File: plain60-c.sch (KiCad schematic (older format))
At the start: 176 parts, among them J1 HRO-TYPE-C-31-M-12, J2 ISP, K1 KEYSW, K10 KEYSW, K11 KEYSW, K12 KEYSW, K13 KEYSW, K14 KEYSW, K15 KEYSW, K15-1 KEYSW, K16 KEYSW, K17 KEYSW, K18 KEYSW, K19 KEYSW, K2 KEYSW, K20 KEYSW, K21 KEYSW, K22 KEYSW, K23 KEYSW, K24 KEYSW, K25 KEYSW, K26 KEYSW, K27 KEYSW, K28 KEYSW, K29 KEYSW, K3 KEYSW, K31 KEYSW, K31-1 KEYSW, K32 KEYSW, K33 KEYSW, K34 KEYSW, K35 KEYSW, K36 KEYSW, K37 KEYSW, K38 KEYSW, K39 KEYSW, K4 KEYSW, K40 KEYSW, K41 KEYSW, K42 KEYSW, K43 KEYSW, K44 KEYSW, K44-1 KEYSW, K46 KEYSW, K46-1 KEYSW, K47 KEYSW, K48 KEYSW, K49 KEYSW, K5 KEYSW, K50 KEYSW, K51 KEYSW, K52 KEYSW, K53 KEYSW, K54 KEYSW, K55 KEYSW, K56 KEYSW, K57 KEYSW, K58 KEYSW, K58-1 KEYSW, K59 KEYSW, K6 KEYSW, K61 KEYSW, K61-1 KEYSW, K62 KEYSW, K62-1 KEYSW, K63 KEYSW, K63-1 KEYSW, K67 KEYSW, K67-1 KEYSW, K7 KEYSW, K71 KEYSW, K72 KEYSW, K72-1 KEYSW, K73 KEYSW, K73-1 KEYSW, K74 KEYSW, K74-1 KEYSW, K8 KEYSW, K9 KEYSW, SW1 SW_PUSH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

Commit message: rescue
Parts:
- J1: symbol Type-C:HRO-TYPE-C-31-M-12 -> plain60-c-rescue:HRO-TYPE-C-31-M-12-Type-C
- K1, K10, K11, K12, K13, K14, K15, K15-1, K16, K17, K18, K19, K2, K20, K21, K22, K23, K24, K25, K26, K27, K28, K29, K3, K31, K31-1, K32, K33, K34, K35, K36, K37, K38, K39, K4, K40, K41, K42, K43, K44, K44-1, K46, K46-1, K47, K48, K49, K5, K50, K51, K52, K53, K54, K55, K56, K57, K58, K58-1, K59, K6, K61, K61-1, K62, K62-1, K63, K63-1, K67, K67-1, K7, K71, K72, K72-1, K73, K73-1, K74, K74-1, K8, K9: symbol keyboard_parts:KEYSW -> plain60-c-rescue:KEYSW-keyboard_parts
- SW1: symbol keyboard_parts:SW_PUSH -> plain60-c-rescue:SW_PUSH-keyboard_parts
- U1: symbol atmel:ATmega32U4 -> plain60-c-rescue:ATmega32U4-atmel
- U2: symbol keyboard_parts:USBLC6-2SC6 -> plain60-c-rescue:USBLC6-2SC6-keyboard_parts
- X1: symbol keyboard_parts:XTAL_GND -> plain60-c-rescue:XTAL_GND-keyboard_parts

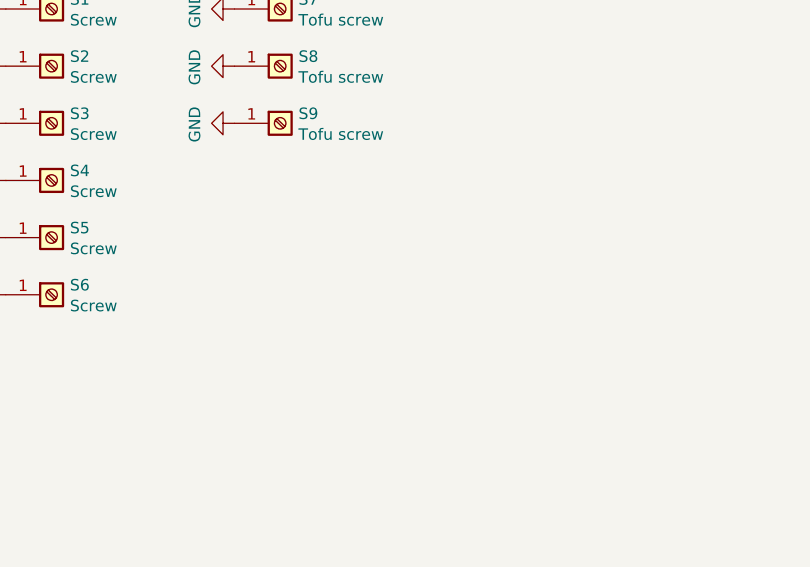
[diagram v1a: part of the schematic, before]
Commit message: add pwr_flag.
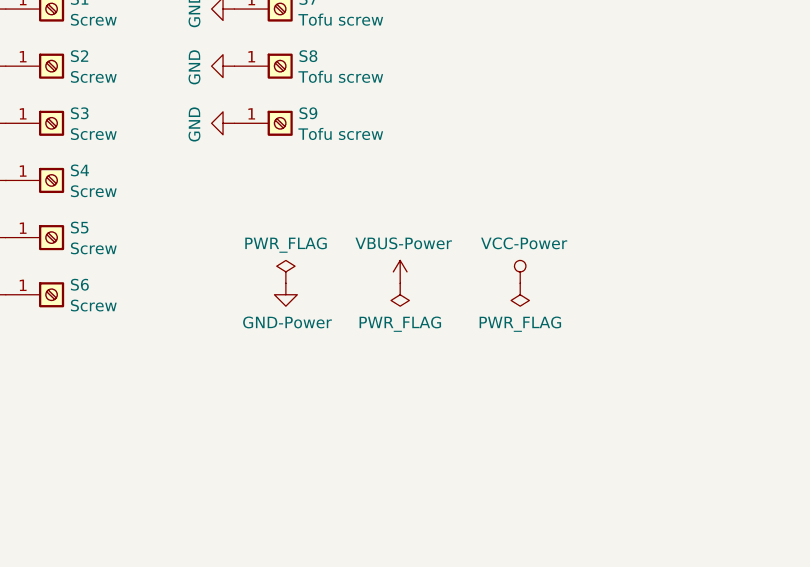
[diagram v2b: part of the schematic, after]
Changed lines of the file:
@@
 Wire Wire Line
 	2150 2850 2150 3750
+$Comp
+L plain60-c-rescue:GND-Power #PWR0130
+U 1 1 5D177425
+P 10275 2200
+F 0 "#PWR0130" H 10275 1950 50  0001 C CNN
+F 1 "GND-Power" H 10280 2027 50  0000 C CNN
+F 2 "" H 10275 2200 50  0001 C CNN
+F 3 "" H 10275 2200 50  0001 C CNN
+	1    10275 2200
+	1    0    0    -1
+$EndComp
+$Comp
+L power:PWR_FLAG #FLG0101
+U 1 1 5D177D5C
+P 10275 2200
+F 0 "#FLG0101" H 10275 2275 50  0001 C CNN
+F 1 "PWR_FLAG" H 10275 2373 50  0000 C CNN
+F 2 "" H 10275 2200 50  0001 C CNN
+F 3 "~" H 10275 2200 50  0001 C CNN
+	1    10275 2200
+	1    0    0    -1
+$EndComp
+$Comp
+L plain60-c-rescue:VBUS-Power #PWR0131
+U 1 1 5D17A18E
+P 10775 2200
+F 0 "#PWR0131" H 10775 2050 50  0001 C CNN
+F 1 "VBUS-Power" H 10790 2373 50  0000 C CNN
+F 2 "" H 10775 2200 50  0001 C CNN
+F 3 "" H 10775 2200 50  0001 C CNN
+	1    10775 2200
+	1    0    0    -1
+$EndComp
+$Comp
+L power:PWR_FLAG #FLG0102
+U 1 1 5D17AA05
+P 10775 2200
+F 0 "#FLG0102" H 10775 2275 50  0001 C CNN
+F 1 "PWR_FLAG" H 10775 2373 50  0000 C CNN
+F 2 "" H 10775 2200 50  0001 C CNN
+F 3 "~" H 10775 2200 50  0001 C CNN
+	1    10775 2200
+	-1   0    0    1
+$EndComp
+$Comp
+L plain60-c-rescue:VCC-Power #PWR0132
+U 1 1 5D17DDD0
+P 11300 2200
+F 0 "#PWR0132" H 11300 2050 50  0001 C CNN
+F 1 "VCC-Power" H 11317 2373 50  0000 C CNN
+F 2 "" H 11300 2200 50  0001 C CNN
+F 3 "" H 11300 2200 50  0001 C CNN
+	1    11300 2200
+	1    0    0    -1
+$EndComp
+$Comp
+L power:PWR_FLAG #FLG0103
+U 1 1 5D17F308
+P 11300 2200
+F 0 "#FLG0103" H 11300 2275 50  0001 C CNN
+F 1 "PWR_FLAG" H 11300 2373 50  0000 C CNN
+F 2 "" H 11300 2200 50  0001 C CNN
+F 3 "~" H 11300 2200 50  0001 C CNN
+	1    11300 2200
+	-1   0    0    1
+$EndComp
 $EndSCHEMATC

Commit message: remove components.
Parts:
- removed C1, C2: 22p, Keeb_components:C_0805, symbol Device:C
- removed C3: 1u, Keeb_components:C_0805, symbol Device:C
- removed C4, C5, C6, C7: 0.1u, Keeb_components:C_0805, symbol Device:C
- removed C8: 4.7u, Keeb_components:C_0805, symbol Device:C
- removed D1, D10, D11, D12, D13, D14, D15, D16, D17, D18, D19, D2, D20, D21, D22, D23, D24, D25, D26, D27, D28, D29, D3, D31, D32, D33, D34, D35, D36, D37, D38, D39, D4, D40, D41, D42, D43, D44, D46, D47, D48, D49, D5, D50, D51, D52, D53, D54, D55, D56, D57, D58, D59, D6, D61, D62, D63, D67, D7, D71, D72, D73, D74, D8, D9: D, Keeb_components:D_0805, symbol Device:D
- removed F1: Polyfuse, Keeb_components:R_0805, symbol Device:Polyfuse
- removed H1: B7, footprints:free_pin, symbol Connector_Generic:Conn_01x01
- removed H2: B0, footprints:free_pin, symbol Connector_Generic:Conn_01x01
- removed H3: GND, footprints:free_pin, symbol Connector_Generic:Conn_01x01
- removed H4: +5v, footprints:free_pin, symbol Connector_Generic:Conn_01x01
- removed J1: HRO-TYPE-C-31-M-12, Keeb_components:HRO-TYPE-C-31-M-12, symbol plain60-c-rescue:HRO-TYPE-C-31-M-12-Type-C
- removed J2: ISP, Keeb_components:isp_standard, symbol Connector_Generic:Conn_02x03_Odd_Even
- removed K1, K10, K11, K12, K13, K14, K15-1, K17, K18, K19, K2, K20, K21, K22, K23, K24, K25, K26, K27, K28, K3, K32, K33, K34, K35, K36, K37, K38, K39, K4, K40, K41, K42, K43, K47, K48, K49, K5, K50, K51, K52, K53, K54, K55, K56, K57, K59, K6, K62-1, K7, K73-1, K8, K9: KEYSW, Keeb_switches:CHERRY_PLATE_100H, symbol plain60-c-rescue:KEYSW-keyboard_parts
- removed K15: KEYSW, Keeb_switches:CHERRY_PCB_200H, symbol plain60-c-rescue:KEYSW-keyboard_parts
- removed K16, K29, K61-1, K63-1, K72-1, K74-1: KEYSW, Keeb_switches:CHERRY_PLATE_150H, symbol plain60-c-rescue:KEYSW-keyboard_parts
- removed K31, K58-1: KEYSW, Keeb_switches:CHERRY_PLATE_175H, symbol plain60-c-rescue:KEYSW-keyboard_parts
- removed K31-1, K46-1, K61, K62, K63, K71, K72, K73, K74: KEYSW, Keeb_switches:CHERRY_PLATE_125H, symbol plain60-c-rescue:KEYSW-keyboard_parts
- removed K44, K46: KEYSW, Keeb_switches:CHERRY_PCB_225H, symbol plain60-c-rescue:KEYSW-keyboard_parts
- removed K44-1: KEYSW, Keeb_switches:CHERRY_PCB_200H_V, symbol plain60-c-rescue:KEYSW-keyboard_parts
- removed K58: KEYSW, Keeb_switches:CHERRY_PCB_275H, symbol plain60-c-rescue:KEYSW-keyboard_parts
- removed K67: KEYSW, Keeb_switches:CHERRY_PCB_625H_F, symbol plain60-c-rescue:KEYSW-keyboard_parts
- removed K67-1: KEYSW, Keeb_switches:CHERRY_PCB_700H_F, symbol plain60-c-rescue:KEYSW-keyboard_parts
- removed R1, R2: 22, Keeb_components:R_0805, symbol Device:R
- removed R3, R4: 5.1k, Keeb_components:R_0805, symbol Device:R
- removed R5, R6: 10k, Keeb_components:R_0805, symbol Device:R
- removed SW1: SW_PUSH, Button_Switch_SMD:SW_SPST_TL3342, symbol plain60-c-rescue:SW_PUSH-keyboard_parts
- removed U1: ATmega32U4, Keeb_components:ATMEGA32U4, symbol plain60-c-rescue:ATmega32U4-atmel
- removed U2: USBLC6-2SC6, Keeb_components:USBLC6-2SC6, symbol plain60-c-rescue:USBLC6-2SC6-keyboard_parts
- removed X1: XTAL_GND, Keeb_components:crystal_FA238-TSX3225, symbol plain60-c-rescue:XTAL_GND-keyboard_parts
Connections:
- no-connect marks 3 -> 0
